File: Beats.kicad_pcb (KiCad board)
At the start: 2 copper layers, 60 x 106.5 mm, 0 parts

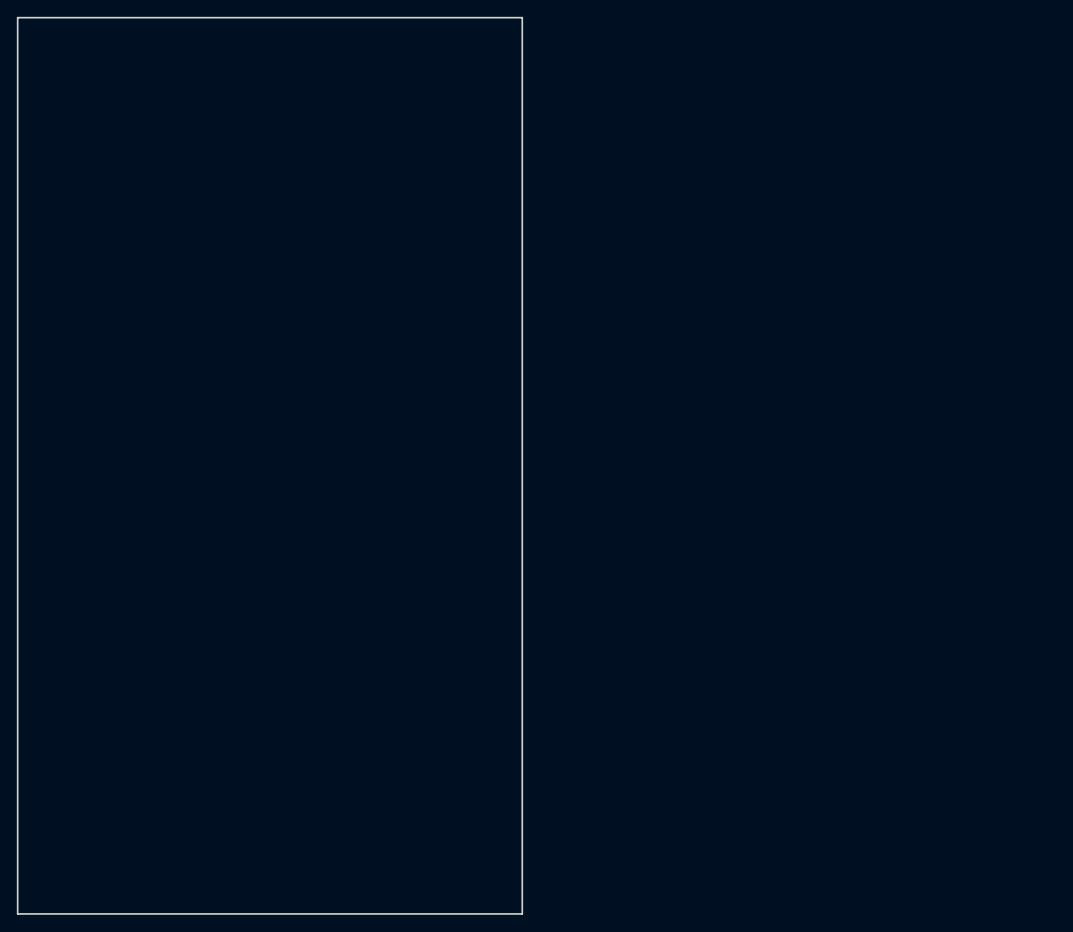
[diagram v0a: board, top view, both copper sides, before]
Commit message: Initial pin assignments and placement.
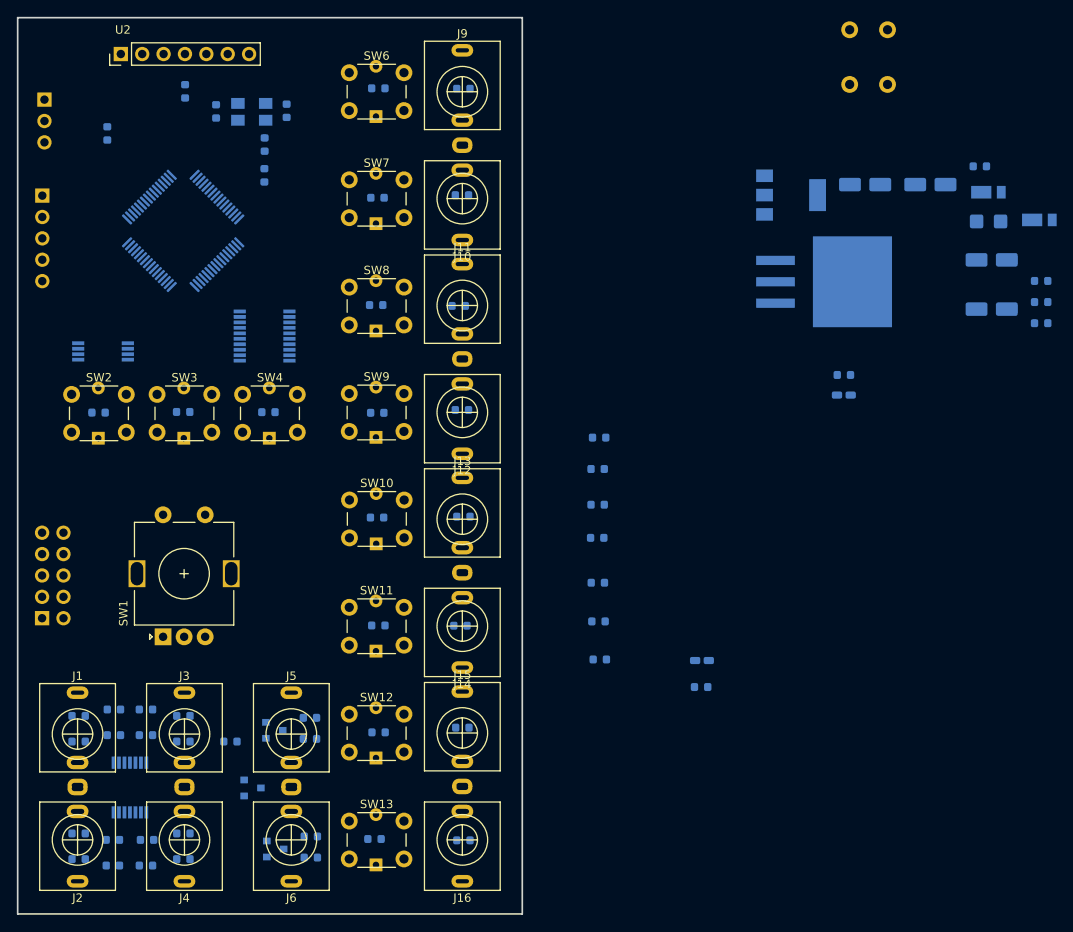
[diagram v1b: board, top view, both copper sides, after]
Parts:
- added C1: 470p, Capacitor_SMD:C_0603_1608Metric, B.Cu at (135.1, 129.0)
- added C10: 100n, Capacitor_SMD:C_0603_1608Metric, B.Cu at (188.8, 108.6)
- added C11: 100n, Capacitor_SMD:C_0603_1608Metric, B.Cu at (188.9, 118.5)
- added C12: 100n, Capacitor_SMD:C_0603_1608Metric, B.Cu at (188.8, 104.6)
- added C13: 100n, Capacitor_SMD:C_0603_1608Metric, B.Cu at (188.8, 100.4)
- added C14: 100n, Capacitor_SMD:C_0603_1608Metric, B.Cu at (189.1, 123.0)
- added C15: 10u, Capacitor_SMD:CP_Elec_4x5.8, B.Cu at (235.6, 75.5)
- added C16: 10u, Capacitor_SMD:CP_Elec_4x5.8, B.Cu at (228.3, 66.6)
- added C17: 100n, Capacitor_SMD:C_0603_1608Metric, B.Cu at (234.2, 64.4)
- added C18: 100n, Capacitor_SMD:C_0603_1608Metric, B.Cu at (241.5, 78.0)
- added C19: 100n, Capacitor_SMD:C_0603_1608Metric, B.Cu at (241.5, 80.5)
- added C2: 470p, Capacitor_SMD:C_0603_1608Metric, B.Cu at (131.3, 129.0)
- added C20: 10u, Capacitor_SMD:CP_Elec_4x5.8, B.Cu at (235.6, 81.4)
- added C21: 10u, Capacitor_SMD:CP_Elec_4x5.8, B.Cu at (220.6, 66.6)
- added C3: 470p, Capacitor_SMD:C_0603_1608Metric, B.Cu at (135.1, 147.5)
- added C4: 470p, Capacitor_SMD:C_0603_1608Metric, B.Cu at (131.2, 147.5)
- added C5: 27p, Capacitor_SMD:C_0603_1608Metric, B.Cu at (143.5, 57.9)
- added C6: 27p, Capacitor_SMD:C_0603_1608Metric, B.Cu at (151.9, 57.8)
- added C7: 100n, Capacitor_SMD:C_0603_1608Metric, B.Cu at (149.2, 65.5)
- added C8: 10n, Capacitor_SMD:C_0603_1608Metric, B.Cu at (188.8, 113.9)
- added C9: 100n, Capacitor_SMD:C_0603_1608Metric, B.Cu at (189.0, 96.6)
- added D1: LED, LED_SMD:LED_0603_1608Metric_Castellated, B.Cu at (201.2, 123.1)
- added D2: LED, LED_SMD:LED_0603_1608Metric_Castellated, B.Cu at (218.1, 91.6)
- added D3: LM4040DBZ-10, Package_TO_SOT_SMD:SOT-23, B.Cu at (147.8, 138.3)
- added D4: DFLR1400-7, Diode_SMD:D_PowerDI-123, B.Cu at (241.3, 70.8)
- added D5: DFLR1400-7, Diode_SMD:D_PowerDI-123, B.Cu at (235.2, 67.5)
- added D6: LED, LED_SMD:LED_1206_3216Metric_Castellated, B.Cu at (235.3, 71.0)
- added J1: AudioJack2_SwitchT, Local.pretty:PJ398SM, F.Cu at (127.0, 131.9)
- added J10: AudioJack2_SwitchT, Local.pretty:PJ398SM, F.Cu at (172.7, 68.2)
- added J11: AudioJack2_SwitchT, Local.pretty:PJ398SM, F.Cu at (172.7, 81.0)
- added J12: AudioJack2_SwitchT, Local.pretty:PJ398SM, F.Cu at (172.7, 93.7)
- added J13: AudioJack2_SwitchT, Local.pretty:PJ398SM, F.Cu at (172.7, 106.3)
- added J14: AudioJack2_SwitchT, Local.pretty:PJ398SM, F.Cu at (172.7, 119.0)
- added J15: AudioJack2_SwitchT, Local.pretty:PJ398SM, F.Cu at (172.7, 131.8)
- added J16: AudioJack2_SwitchT, Local.pretty:PJ398SM, F.Cu at (172.7, 144.4)
- added J17: Conn_02x05_Odd_Even, Connector_PinHeader_2.54mm:PinHeader_2x05_P2.54mm_Vertical, B.Cu at (122.8, 118.1)
- added J2: AudioJack2_SwitchT, Local.pretty:PJ398SM, F.Cu at (127.0, 144.4)
- added J3: AudioJack2_SwitchT, Local.pretty:PJ398SM, F.Cu at (139.7, 131.9)
- added J4: AudioJack2_SwitchT, Local.pretty:PJ398SM, F.Cu at (139.7, 144.4)
- added J5: AudioJack2_SwitchT, Local.pretty:PJ398SM, F.Cu at (152.4, 131.9)
- added J6: AudioJack2_SwitchT, Local.pretty:PJ398SM, F.Cu at (152.4, 144.4)
- added J7: SWD, Connector_PinHeader_2.54mm:PinHeader_1x05_P2.54mm_Vertical, B.Cu at (122.8, 67.9)
- added J8: Conn_01x03_Male, Connector_PinHeader_2.54mm:PinHeader_1x03_P2.54mm_Vertical, B.Cu at (123.1, 56.5)
- added J9: AudioJack2_SwitchT, Local.pretty:PJ398SM, F.Cu at (172.7, 55.5)
- added Q1: BC847, Package_TO_SOT_SMD:SOT-23, B.Cu at (150.4, 131.4)
- added Q2: BC847, Package_TO_SOT_SMD:SOT-23, B.Cu at (150.5, 145.5)
- added R1: 200k, Resistor_SMD:R_0603_1608Metric, B.Cu at (139.6, 132.8)
- added R10: 33k, Resistor_SMD:R_0603_1608Metric, B.Cu at (135.1, 132.0)
- added R11: 33k, Resistor_SMD:R_0603_1608Metric, B.Cu at (135.3, 144.4)
- added R12: 33k, Resistor_SMD:R_0603_1608Metric, B.Cu at (131.2, 144.4)
- added R13: 330, Resistor_SMD:R_0603_1608Metric, B.Cu at (201.1, 126.3)
- added R14: 330, Resistor_SMD:R_0603_1608Metric, B.Cu at (218.1, 89.2)
- added R15: 150, Resistor_SMD:R_0603_1608Metric, B.Cu at (129.5, 93.7)
- added R16: 150, Resistor_SMD:R_0603_1608Metric, B.Cu at (139.6, 93.6)
- added R17: 150, Resistor_SMD:R_0603_1608Metric, B.Cu at (149.7, 93.6)
- added R18: 10k, Resistor_SMD:R_0603_1608Metric, B.Cu at (130.5, 60.5)
- added R19: 470, Resistor_SMD:R_0603_1608Metric, B.Cu at (149.2, 61.8)
- added R2: 100k, Resistor_SMD:R_0603_1608Metric, B.Cu at (139.6, 129.7)
- added R20: 1k, Resistor_SMD:R_0603_1608Metric, B.Cu at (139.8, 55.5)
- added R21: 150, Resistor_SMD:R_0603_1608Metric, B.Cu at (162.8, 55.1)
- added R22: 150, Resistor_SMD:R_0603_1608Metric, B.Cu at (162.6, 68.1)
- added R23: 150, Resistor_SMD:R_0603_1608Metric, B.Cu at (162.5, 80.9)
- added R24: 150, Resistor_SMD:R_0603_1608Metric, B.Cu at (162.6, 93.7)
- added R25: 150, Resistor_SMD:R_0603_1608Metric, B.Cu at (162.6, 106.1)
- added R26: 150, Resistor_SMD:R_0603_1608Metric, B.Cu at (162.8, 119.0)
- added R27: 150, Resistor_SMD:R_0603_1608Metric, B.Cu at (162.8, 131.7)
- added R28: 150, Resistor_SMD:R_0603_1608Metric, B.Cu at (162.3, 144.3)
- added R29: 1k, Resistor_SMD:R_0603_1608Metric, B.Cu at (172.9, 55.2)
- added R3: 200k, Resistor_SMD:R_0603_1608Metric, B.Cu at (127.1, 132.8)
- added R30: 1k, Resistor_SMD:R_0603_1608Metric, B.Cu at (172.7, 67.8)
- added R31: 1k, Resistor_SMD:R_0603_1608Metric, B.Cu at (172.3, 81.0)
- added R32: 1k, Resistor_SMD:R_0603_1608Metric, B.Cu at (172.7, 93.4)
- added R33: 1k, Resistor_SMD:R_0603_1608Metric, B.Cu at (172.9, 106.0)
- added R34: 1k, Resistor_SMD:R_0603_1608Metric, B.Cu at (172.5, 119.0)
- added R35: 1k, Resistor_SMD:R_0603_1608Metric, B.Cu at (172.7, 131.1)
- added R36: 1k, Resistor_SMD:R_0603_1608Metric, B.Cu at (172.9, 144.5)
- added R37: 2k2, Resistor_SMD:R_0603_1608Metric, B.Cu at (145.2, 132.8)
- added R38: 330, Resistor_SMD:R_0603_1608Metric, B.Cu at (241.5, 83.1)
- added R39: 100k, Resistor_SMD:R_0603_1608Metric, B.Cu at (154.6, 129.9)
- added R4: 100k, Resistor_SMD:R_0603_1608Metric, B.Cu at (127.1, 129.7)
- added R40: 10k, Resistor_SMD:R_0603_1608Metric, B.Cu at (154.6, 132.5)
- added R41: 100k, Resistor_SMD:R_0603_1608Metric, B.Cu at (154.7, 144.0)
- added R42: 10k, Resistor_SMD:R_0603_1608Metric, B.Cu at (154.7, 146.6)
- added R5: 200k, Resistor_SMD:R_0603_1608Metric, B.Cu at (139.6, 143.7)
- added R6: 100k, Resistor_SMD:R_0603_1608Metric, B.Cu at (139.6, 146.7)
- added R7: 200k, Resistor_SMD:R_0603_1608Metric, B.Cu at (127.1, 143.7)
- added R8: 100k, Resistor_SMD:R_0603_1608Metric, B.Cu at (127.1, 146.7)
- added R9: 33k, Resistor_SMD:R_0603_1608Metric, B.Cu at (131.3, 132.0)
- added SW1: Rotary_Encoder_Switch, Rotary_Encoder:RotaryEncoder_Alps_EC11E-Switch_Vertical_H20mm, F.Cu at (137.2, 120.3)
- added SW10: SW_Push_LED, Local.pretty:SW_PUSH_LED_6mm, F.Cu at (162.5, 106.3)
- added SW11: SW_Push_LED, Local.pretty:SW_PUSH_LED_6mm, F.Cu at (162.5, 119.1)
- added SW12: SW_Push_LED, Local.pretty:SW_PUSH_LED_6mm, F.Cu at (162.5, 131.8)
- added SW13: SW_Push_LED, Local.pretty:SW_PUSH_LED_6mm, F.Cu at (162.5, 144.5)
- added SW2: SW_Push_LED, Local.pretty:SW_PUSH_LED_6mm, F.Cu at (129.5, 93.8)
- added SW3: SW_Push_LED, Local.pretty:SW_PUSH_LED_6mm, F.Cu at (139.6, 93.8)
- added SW4: SW_Push_LED, Local.pretty:SW_PUSH_LED_6mm, F.Cu at (149.8, 93.8)
- added SW5: SW_Push, Button_Switch_THT:SW_PUSH_6mm, B.Cu at (218.8, 48.2)
- added SW6: SW_Push_LED, Local.pretty:SW_PUSH_LED_6mm, F.Cu at (162.5, 55.6)
- added SW7: SW_Push_LED, Local.pretty:SW_PUSH_LED_6mm, F.Cu at (162.5, 68.3)
- added SW8: SW_Push_LED, Local.pretty:SW_PUSH_LED_6mm, F.Cu at (162.5, 81.1)
- added SW9: SW_Push_LED, Local.pretty:SW_PUSH_LED_6mm, F.Cu at (162.5, 93.7)
- added U1: MCP6004, Package_SO:TSSOP-14_4.4x5mm_P0.65mm, B.Cu at (133.2, 138.2)
- added U2: IPS240x240, Local.pretty:IPS240x240, F.Cu at (139.8, 69.2)
- added U3: STM32F051R8Tx, Package_QFP:LQFP-64_10x10mm_P0.5mm, B.Cu at (139.6, 72.1)
- added U4: AT25xxx, Package_SO:TSSOP-8_4.4x3mm_P0.65mm, B.Cu at (130.0, 86.4)
- added U5: 74AHCT244, Package_SO:TSSOP-20_4.4x6.5mm_P0.65mm, B.Cu at (149.2, 84.6)
- added U6: L7805, Package_TO_SOT_SMD:SOT-223-3_TabPin2, B.Cu at (211.8, 67.8)
- added U7: LM1117-3.3, Package_TO_SOT_SMD:TO-263-3_TabPin2, B.Cu at (215.7, 78.1)
- added Y1: 8MHz, Crystal:Crystal_SMD_5032-4Pin_5.0x3.2mm, B.Cu at (147.7, 57.9)

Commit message: Added UART and corresponding pin assignments.
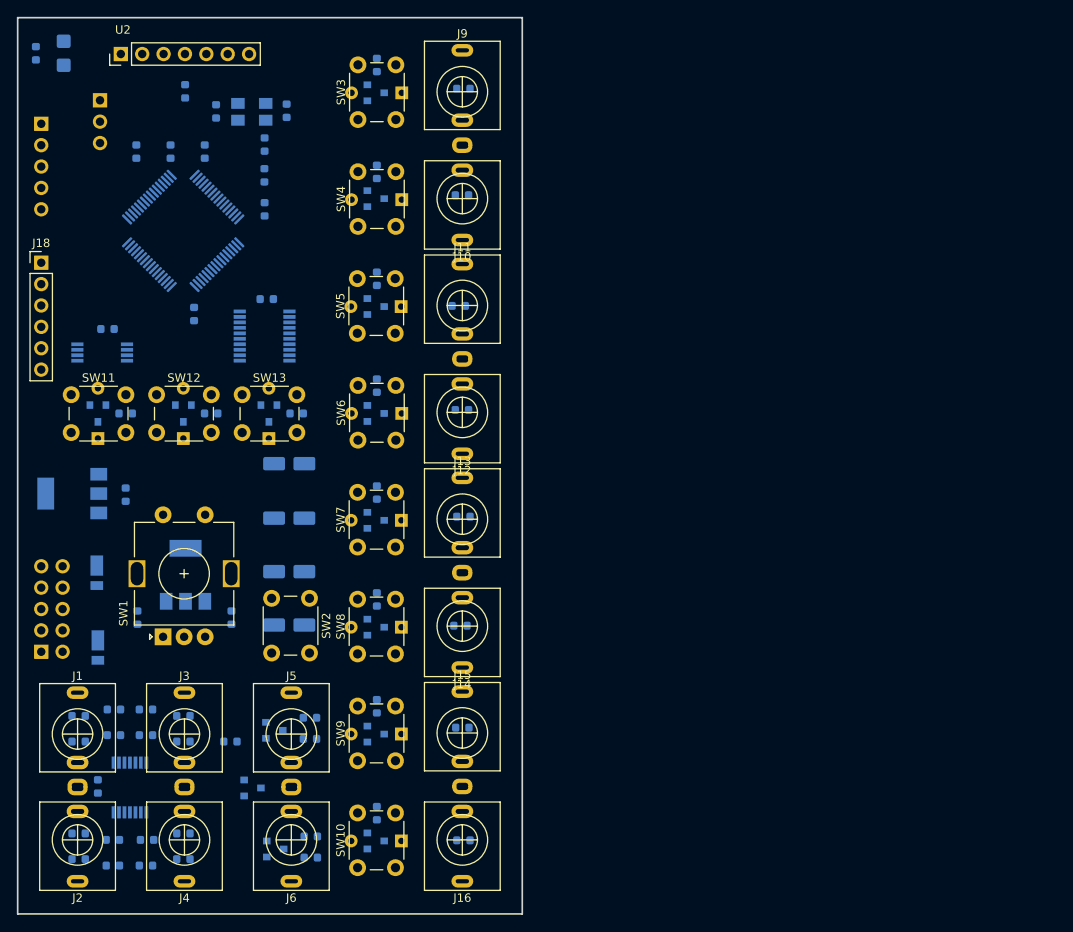
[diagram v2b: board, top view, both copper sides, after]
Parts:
- removed the D1 at (201.2, 123.1)
- removed the D2 at (218.1, 91.6)
- removed the R13 at (201.1, 126.3)
- removed the R14 at (218.1, 89.2)
- removed the R15 at (129.5, 93.7)
- removed the R16 at (139.6, 93.6)
- removed the R17 at (149.7, 93.6)
- removed the R21 at (162.8, 55.1)
- removed the R22 at (162.6, 68.1)
- removed the R23 at (162.5, 80.9)
- removed the R24 at (162.6, 93.7)
- removed the R25 at (162.6, 106.1)
- removed the R26 at (162.8, 119.0)
- removed the R27 at (162.8, 131.7)
- removed the R28 at (162.3, 144.3)
- added J18: UART, Connector_PinHeader_2.54mm:PinHeader_1x06_P2.54mm_Vertical, F.Cu at (122.7, 75.9)
- added Q10: BC847, Package_TO_SOT_SMD:SOT-23, B.Cu at (162.4, 144.6)
- added Q11: BC847, Package_TO_SOT_SMD:SOT-23, B.Cu at (129.4, 93.8)
- added Q12: BC847, Package_TO_SOT_SMD:SOT-23, B.Cu at (139.6, 93.8)
- added Q13: BC847, Package_TO_SOT_SMD:SOT-23, B.Cu at (149.7, 93.8)
- added Q3: BC847, Package_TO_SOT_SMD:SOT-23, B.Cu at (162.4, 55.7)
- added Q4: BC847, Package_TO_SOT_SMD:SOT-23, B.Cu at (162.4, 68.2)
- added Q5: BC847, Package_TO_SOT_SMD:SOT-23, B.Cu at (162.4, 81.1)
- added Q6: BC847, Package_TO_SOT_SMD:SOT-23, B.Cu at (162.4, 93.8)
- added Q7: BC847, Package_TO_SOT_SMD:SOT-23, B.Cu at (162.4, 106.5)
- added Q8: BC847, Package_TO_SOT_SMD:SOT-23, B.Cu at (162.4, 119.2)
- added Q9: BC847, Package_TO_SOT_SMD:SOT-23, B.Cu at (162.4, 131.9)
- added R30: 47, Resistor_SMD:R_0603_1608Metric, B.Cu at (162.6, 52.4)
- added R31: 47, Resistor_SMD:R_0603_1608Metric, B.Cu at (162.6, 65.1)
- added R32: 47, Resistor_SMD:R_0603_1608Metric, B.Cu at (162.6, 77.8)
- added R33: 47, Resistor_SMD:R_0603_1608Metric, B.Cu at (162.6, 90.5)
- added R34: 47, Resistor_SMD:R_0603_1608Metric, B.Cu at (162.6, 103.2)
- added R35: 47, Resistor_SMD:R_0603_1608Metric, B.Cu at (162.6, 115.9)
- added R36: 47, Resistor_SMD:R_0603_1608Metric, B.Cu at (162.6, 128.6)
- added R37: 47, Resistor_SMD:R_0603_1608Metric, B.Cu at (162.6, 141.3)
- added R38: 47, Resistor_SMD:R_0603_1608Metric, B.Cu at (132.7, 93.8)
- added R39: 47, Resistor_SMD:R_0603_1608Metric, B.Cu at (142.9, 93.8)
- added R40: 47, Resistor_SMD:R_0603_1608Metric, B.Cu at (153.0, 93.8)
- SW2: value SW_Push_LED -> SW_Push; footprint Local.pretty:SW_PUSH_LED_6mm -> Button_Switch_THT:SW_PUSH_6mm
- SW5: value SW_Push -> SW_Push_LED; footprint Button_Switch_THT:SW_PUSH_6mm -> Local.pretty:SW_PUSH_LED_6mm; moved to F.Cu
- U7: footprint Package_TO_SOT_SMD:TO-263-3_TabPin2 -> Package_TO_SOT_SMD:SOT-223-3_TabPin2
- moved R25 123.7 mm to (122.1, 51.0), turned to 90 degrees
- moved D2 119.6 mm to (129.3, 112.7), turned to 270 degrees
- moved D3 118.8 mm to (129.4, 121.6), turned to 270 degrees
- moved C19 113.7 mm to (134.1, 118.0), turned to 270 degrees
- moved C18 111.7 mm to (132.7, 103.4), turned to 90 degrees
- moved D4 111.7 mm to (125.4, 51.0), turned to 270 degrees
- moved C17 103.8 mm to (145.3, 118.0), turned to 270 degrees
- moved U7 92.8 mm to (126.4, 103.3), turned to 180 degrees
- moved C20 91.5 mm to (152.2, 118.9)
- moved C15 91.3 mm to (152.2, 112.6)
- moved C16 85.9 mm to (152.2, 106.2)
- moved U6 84.9 mm to (139.8, 113.0), turned to 90 degrees
- moved C21 76.0 mm to (152.2, 99.7)
- moved C11 75.5 mm to (138.1, 62.7), turned to 90 degrees
- moved C10 65.4 mm to (142.1, 62.7), turned to 90 degrees
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- renumbered D3 to D1, D4 to D2, D5 to D3, D6 to D4, R18 to R13, R19 to R14, R20 to R15, R29 to R16, R30 to R17, R31 to R18, R32 to R19, R33 to R20, R34 to R21, R35 to R22, R36 to R23, R37 to R24, R38 to R25, R39 to R26, R40 to R27, R41 to R28, R42 to R29
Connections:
- net Net-(SW10-Pad1) renamed /sheet5DB3CABC/SW
- net Net-(SW3-Pad1) renamed /PushLED/SW
- net Net-(SW4-Pad1) renamed /sheet5DAF110B/SW
- net Net-(SW6-Pad1) renamed /sheet5DB16B86/SW
- net Net-(SW7-Pad1) renamed /sheet5DB3CAB0/SW
- net Net-(SW8-Pad1) renamed /sheet5DB3CAB4/SW
- net Net-(SW9-Pad1) renamed /sheet5DB3CAB8/SW
- C1 pad 1: PC4 -> PC0
- C2 pad 1: PC5 -> PC1
- C3 pad 1: PB0 -> PC2
- C4 pad 1: PB1 -> PC3
- R10 pad 1: PC5 -> PC1
- R11 pad 1: PB0 -> PC2
- R12 pad 1: PB1 -> PC3
- R9 pad 1: PC4 -> PC0
- SW1 pad A: PA7 -> Net-(SW1-PadA)
- SW1 pad B: PA6 -> Net-(SW1-PadB)
- SW11 pad 1: Net-(SW11-Pad1) -> PA11
- SW12 pad 1: Net-(SW12-Pad1) -> PC9
- SW13 pad 1: Net-(SW13-Pad1) -> PC7
- SW2 pad 1: Net-(SW2-Pad1) -> GND
- SW2 pad 2: GND -> RESET
- SW5 pad 1: GND -> /sheet5DB16B82/SW
- SW5 pad 2: RESET -> GND
- U1 pad 1: PC4 -> PC0
- U1 pad 14: PB1 -> PC3
- U1 pad 7: PC5 -> PC1
- U1 pad 8: PB0 -> PC2
- U2 pad 6: PB4 -> Net-(U2-Pad6)

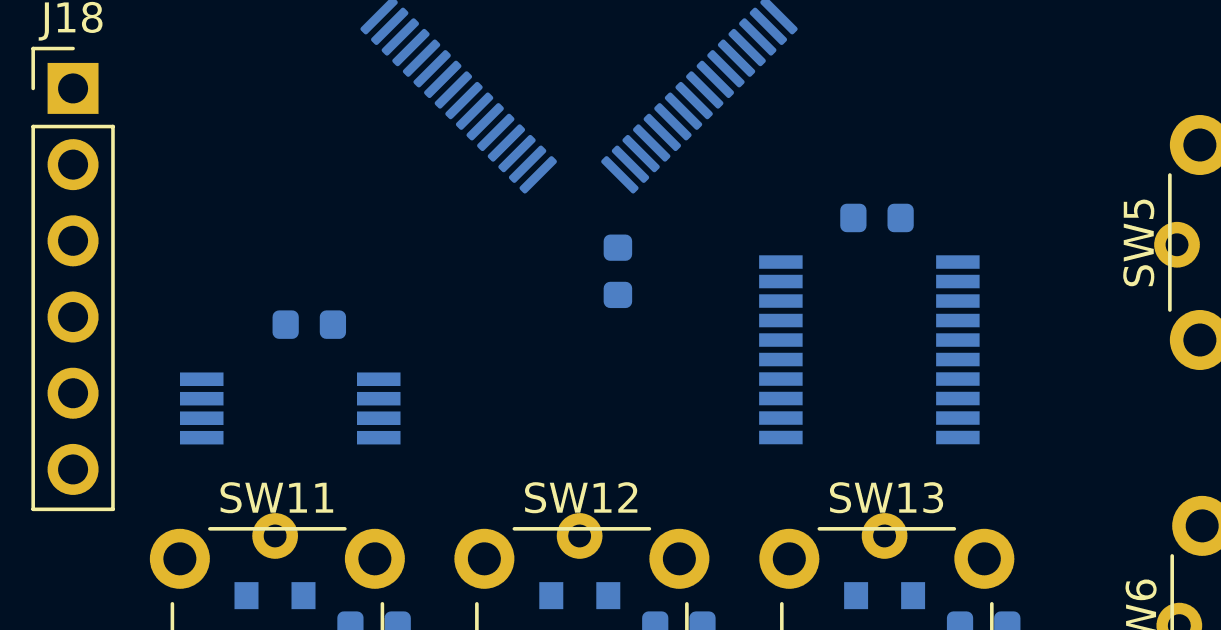
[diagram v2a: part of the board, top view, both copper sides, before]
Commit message: Assigned trigger output pins.
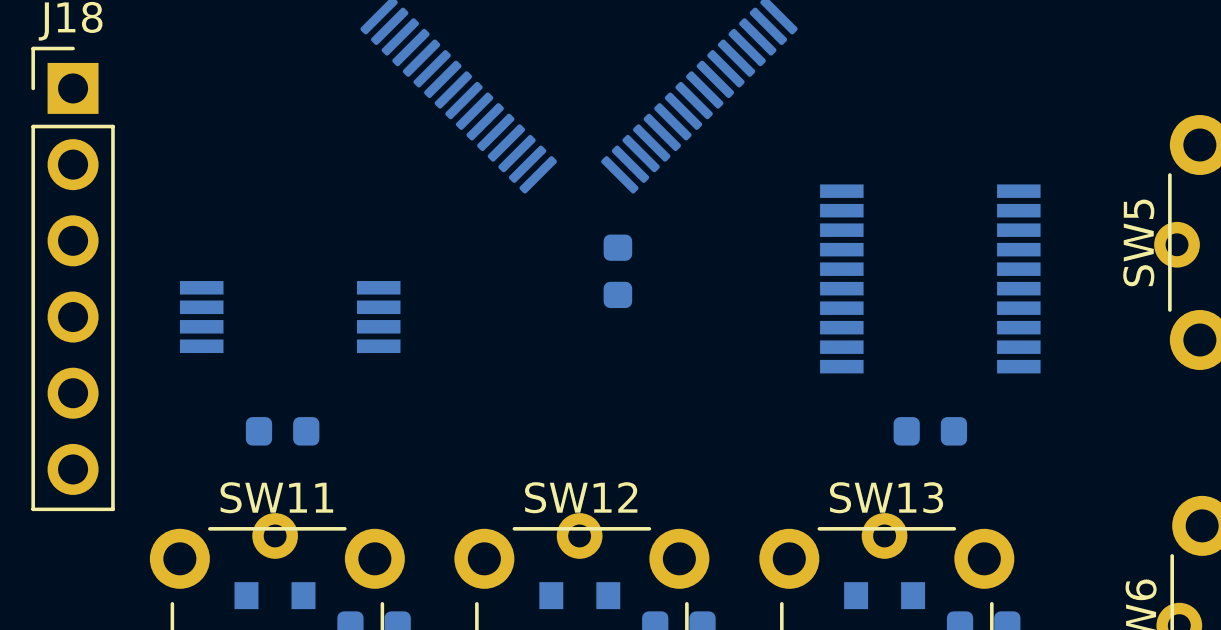
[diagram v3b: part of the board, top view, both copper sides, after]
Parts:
- moved C9 7.33 mm to (151.3, 87.3)
- moved C13 3.67 mm to (129.7, 87.3)
- moved U5 3.12 mm to (151.3, 82.2)
- moved U4 3.05 mm to (129.9, 83.5)
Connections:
- C9 pad 1: +3.3VA -> +5V
- U5 pad 11: Net-(U5-Pad11) -> PB11
- U5 pad 13: Net-(U5-Pad13) -> PB10
- U5 pad 15: Net-(U5-Pad15) -> PB2
- U5 pad 17: Net-(U5-Pad17) -> PB1
- U5 pad 2: Net-(U5-Pad2) -> PA7
- U5 pad 4: Net-(U5-Pad4) -> PC4
- U5 pad 6: Net-(U5-Pad6) -> PC5
- U5 pad 8: Net-(U5-Pad8) -> PB0

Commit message: Corrected port collisions.
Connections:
- C1 pad 1: PC0 -> PC4
- C2 pad 1: PC1 -> PC5
- C3 pad 1: PC2 -> PB0
- C4 pad 1: PC3 -> PB1
- R10 pad 1: PC1 -> PC5
- R11 pad 1: PC2 -> PB0
- R12 pad 1: PC3 -> PB1
- R9 pad 1: PC0 -> PC4
- SW1 pad A: Net-(SW1-PadA) -> PA7
- SW1 pad B: Net-(SW1-PadB) -> PA6
- U1 pad 1: PC0 -> PC4
- U1 pad 14: PC3 -> PB1
- U1 pad 7: PC1 -> PC5
- U1 pad 8: PC2 -> PB0
- U5 pad 17: PB1 -> PA5
- U5 pad 2: PA7 -> PA3
- U5 pad 4: PC4 -> PF4
- U5 pad 6: PC5 -> PF5
- U5 pad 8: PB0 -> PA4
